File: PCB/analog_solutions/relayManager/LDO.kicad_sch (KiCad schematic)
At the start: 4 parts, among them U26 L78L05_SOT89

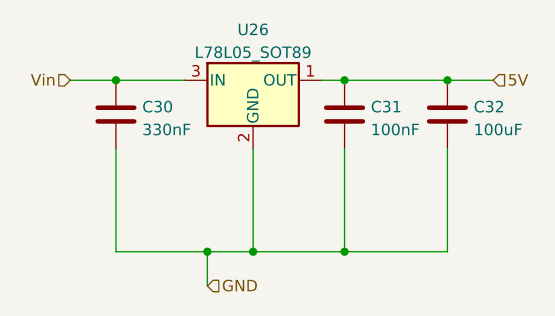
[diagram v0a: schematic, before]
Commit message: made some changed to relay manager
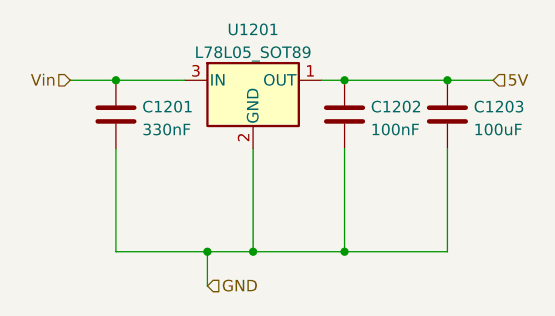
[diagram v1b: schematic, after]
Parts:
- renumbered C30 to C1201, C31 to C1202, C32 to C1203, U26 to U1201
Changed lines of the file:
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@@
   (symbol (lib_id "Device:C") (at 203.2 92.71 0) (unit 1)
     (in_bom yes) (on_board yes) (dnp no) (fields_autoplaced)
-    (property "Reference" "C31" (at 206.121 91.8753 0)
+    (property "Reference" "C1202" (at 206.121 91.8753 0)
       (effects (font (size 1.27 1.27)) (justify left))
     )
@@
   (symbol (lib_id "Regulator_Linear:L78L05_SOT89") (at 193.04 88.9 0) (unit 1)
     (in_bom yes) (on_board yes) (dnp no) (fields_autoplaced)
-    (property "Reference" "U26" (at 193.04 83.2952 0)
+    (property "Reference" "U1201" (at 193.04 83.2952 0)
       (effects (font (size 1.27 1.27)))
     )
@@
   (symbol (lib_id "Device:C") (at 177.8 92.71 0) (unit 1)
     (in_bom yes) (on_board yes) (dnp no) (fields_autoplaced)
-    (property "Reference" "C30" (at 180.721 91.8753 0)
+    (property "Reference" "C1201" (at 180.721 91.8753 0)
       (effects (font (size 1.27 1.27)) (justify left))
     )
@@
   (symbol (lib_id "Device:C") (at 214.63 92.71 0) (unit 1)
     (in_bom yes) (on_board yes) (dnp no) (fields_autoplaced)
-    (property "Reference" "C32" (at 217.551 91.8753 0)
+    (property "Reference" "C1203" (at 217.551 91.8753 0)
       (effects (font (size 1.27 1.27)) (justify left))
     )

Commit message: added production files to xnet block unit
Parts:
- renumbered C1201 to C1101, C1202 to C1102, C1203 to C1103, U1201 to U1101
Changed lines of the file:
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@@
   (symbol (lib_id "Device:C") (at 203.2 92.71 0) (unit 1)
     (in_bom yes) (on_board yes) (dnp no) (fields_autoplaced)
-    (property "Reference" "C1202" (at 206.121 91.8753 0)
+    (property "Reference" "C1102" (at 206.121 91.8753 0)
       (effects (font (size 1.27 1.27)) (justify left))
     )
@@
       (project "relayManager"
         (path "/0f9af3f2-fc8b-411c-8220-6dd1cf876187/a0e78025-7fca-48b5-974d-3df94f918b98"
-          (reference "C1202") (unit 1)
+          (reference "C1102") (unit 1)
         )
       )
@@
   (symbol (lib_id "Regulator_Linear:L78L05_SOT89") (at 193.04 88.9 0) (unit 1)
     (in_bom yes) (on_board yes) (dnp no) (fields_autoplaced)
-    (property "Reference" "U1201" (at 193.04 83.2952 0)
+    (property "Reference" "U1101" (at 193.04 83.2952 0)
       (effects (font (size 1.27 1.27)))
     )
@@
       (project "relayManager"
         (path "/0f9af3f2-fc8b-411c-8220-6dd1cf876187/a0e78025-7fca-48b5-974d-3df94f918b98"
-          (reference "U1201") (unit 1)
+          (reference "U1101") (unit 1)
         )
       )
@@
   (symbol (lib_id "Device:C") (at 177.8 92.71 0) (unit 1)
     (in_bom yes) (on_board yes) (dnp no) (fields_autoplaced)
-    (property "Reference" "C1201" (at 180.721 91.8753 0)
+    (property "Reference" "C1101" (at 180.721 91.8753 0)
       (effects (font (size 1.27 1.27)) (justify left))
     )
@@
       (project "relayManager"
         (path "/0f9af3f2-fc8b-411c-8220-6dd1cf876187/a0e78025-7fca-48b5-974d-3df94f918b98"
-          (reference "C1201") (unit 1)
+          (reference "C1101") (unit 1)
         )
       )
@@
   (symbol (lib_id "Device:C") (at 214.63 92.71 0) (unit 1)
     (in_bom yes) (on_board yes) (dnp no) (fields_autoplaced)
-    (property "Reference" "C1203" (at 217.551 91.8753 0)
+    (property "Reference" "C1103" (at 217.551 91.8753 0)
       (effects (font (size 1.27 1.27)) (justify left))
     )
@@
       (project "relayManager"
         (path "/0f9af3f2-fc8b-411c-8220-6dd1cf876187/a0e78025-7fca-48b5-974d-3df94f918b98"
-          (reference "C1203") (unit 1)
+          (reference "C1103") (unit 1)
         )
       )
